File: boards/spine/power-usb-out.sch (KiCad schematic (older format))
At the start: 9 parts

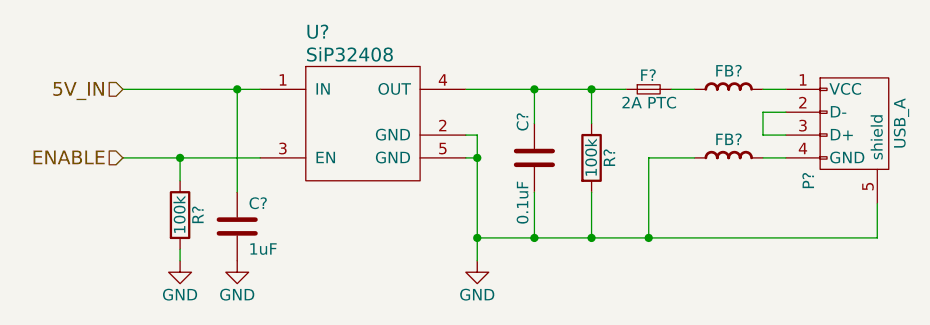
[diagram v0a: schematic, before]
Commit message: Power source switching
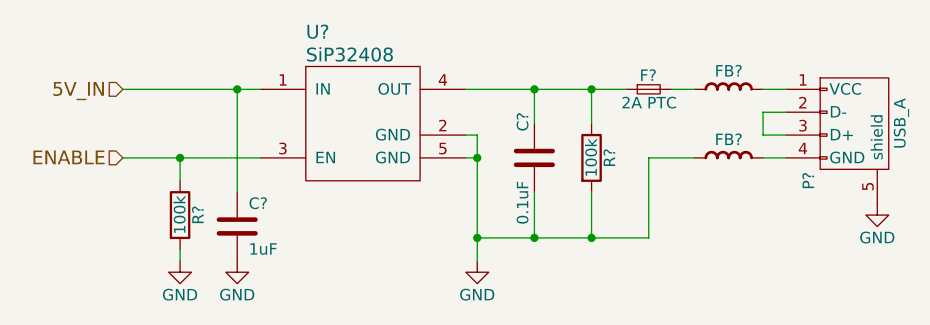
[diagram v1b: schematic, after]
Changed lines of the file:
@@
 	1    0    0    -1
 $EndComp
+$Comp
+L F_Small F?
+U 1 1 564D338C
+P 6400 3700
+F 0 "F?" H 6360 3760 50  0000 L CNN
+F 1 "2A PTC" H 6280 3640 50  0000 L CNN
+F 2 "1812" H 6400 3700 60  0001 C CNN
+F 3 "http://www.belfuse.com/pdfs/0ZCG.pdf" H 6400 3700 60  0001 C CNN
+F 4 "Digikey" H 6400 3700 60  0001 C CNN "Vend1"
+F 5 "507-1777-1-ND" H 6400 3700 60  0001 C CNN "Vend1Id"
+F 6 "Bel Fuse" H 6400 3700 60  0001 C CNN "MfrId"
+F 7 "0ZCG0200FF2C" H 6400 3700 60  0001 C CNN "MfgId"
+F 8 "0.09403" H 6400 3700 60  0001 C CNN "RefPrice1k"
+	1    6400 3700
+	1    0    0    -1
+$EndComp
+Text HLabel 4100 3700 0    60   Input ~ 0
+5V_IN
+Text HLabel 4100 4000 0    60   Input ~ 0
+ENABLE
 Wire Wire Line
 	4350 4450 4350 4400
 Wire Wire Line
-	4100 4000 4350 4000
-Wire Wire Line
-	4350 4000 4700 4000
+	4100 4000 4700 4000
 Wire Wire Line
 	4350 4100 4350 4000
@@
 	5600 4000 5650 4000
 Wire Wire Line
-	5650 3900 5650 4000
-Wire Wire Line
-	5650 4000 5650 4350
-Wire Wire Line
-	5650 4350 5650 4450
+	5650 3900 5650 4450
 Wire Wire Line
 	5600 3900 5650 3900
@@
 Connection ~ 5650 4350
 Wire Wire Line
-	5600 3700 5900 3700
-Wire Wire Line
-	5900 3700 6150 3700
-Wire Wire Line
-	6150 3700 6300 3700
+	5600 3700 6300 3700
 Wire Wire Line
 	5900 3700 5900 3850
@@
 Connection ~ 5900 4350
 Wire Wire Line
-	7400 4350 7400 4200
-Connection ~ 6400 4350
-Wire Wire Line
 	6150 4350 6150 4150
 Connection ~ 6150 4350
@@
 	4600 4150 4600 3700
 Wire Wire Line
-	4100 3700 4600 3700
-Wire Wire Line
-	4600 3700 4700 3700
-$Comp
-L F_Small F?
-U 1 1 564D338C
-P 6400 3700
-F 0 "F?" H 6360 3760 50  0000 L CNN
-F 1 "2A PTC" H 6280 3640 50  0000 L CNN
-F 2 "1812" H 6400 3700 60  0001 C CNN
-F 3 "http://www.belfuse.com/pdfs/0ZCG.pdf" H 6400 3700 60  0001 C CNN
-F 4 "Digikey" H 6400 3700 60  0001 C CNN "Vend1"
-F 5 "507-1777-1-ND" H 6400 3700 60  0001 C CNN "Vend1Id"
-F 6 "Bel Fuse" H 6400 3700 60  0001 C CNN "MfrId"
-F 7 "0ZCG0200FF2C" H 6400 3700 60  0001 C CNN "MfgId"
-F 8 "0.09403" H 6400 3700 60  0001 C CNN "RefPrice1k"
-	1    6400 3700
-	1    0    0    -1
-$EndComp
+	4100 3700 4700 3700
 Wire Wire Line
 	6500 3700 6600 3700
 Wire Wire Line
-	6400 4000 6400 4350
+	6400 4350 6400 4000
+Connection ~ 4600 3700
 Wire Wire Line
-	5650 4350 5900 4350
-Wire Wire Line
-	5900 4350 6150 4350
-Wire Wire Line
-	6150 4350 6400 4350
-Wire Wire Line
-	6400 4350 7400 4350
-Connection ~ 4600 3700
-Text HLabel 4100 3700 0    60   Input ~ 0
-5V_IN
-Text HLabel 4100 4000 0    60   Input ~ 0
-ENABLE
+	5650 4350 6400 4350
+$Comp
+L GND #PWR?
+U 1 1 564CFCD3
+P 7400 4200
+F 0 "#PWR?" H 7400 3950 50  0001 C CNN
+F 1 "GND" H 7400 4050 50  0000 C CNN
+F 2 "" H 7400 4200 60  0000 C CNN
+F 3 "" H 7400 4200 60  0000 C CNN
+	1    7400 4200
+	1    0    0    -1
+$EndComp
 $EndSCHEMATC

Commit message: Power management and such
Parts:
- added C64: 0.1uF, 0805, symbol C
- P3: renamed from P?; value USB_A -> USB-A; MfgId (none) -> USB-A1SSW6; MfrId (none) -> On-Shore Tech; RefPrice1k (none) -> 0.35310; Vend1 (none) -> Digikey; Vend1Id (none) -> ED2991-ND
- U10: renamed from U?; MfgId (none) -> Vishay; MfrId (none) -> SIP32408DNP-T1-GE4; RefPrice1k (none) -> 0.175; Vend1 (none) -> Digikey; Vend1Id (none) -> SIP32408DNP-T1-GE4CT-ND
- gave numbers to parts that had none: 7
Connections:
- net GND: now also C64.1
- net at F1.2, FB5.1: now also C64.2
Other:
- note added: "Not the main +5V rail; this is intended to draw power\nfrom the DC-DC converter only, not the USB-B input."
- moved on the sheet: C62, C63, F1, FB5, FB6, P3, R29, R30, U10

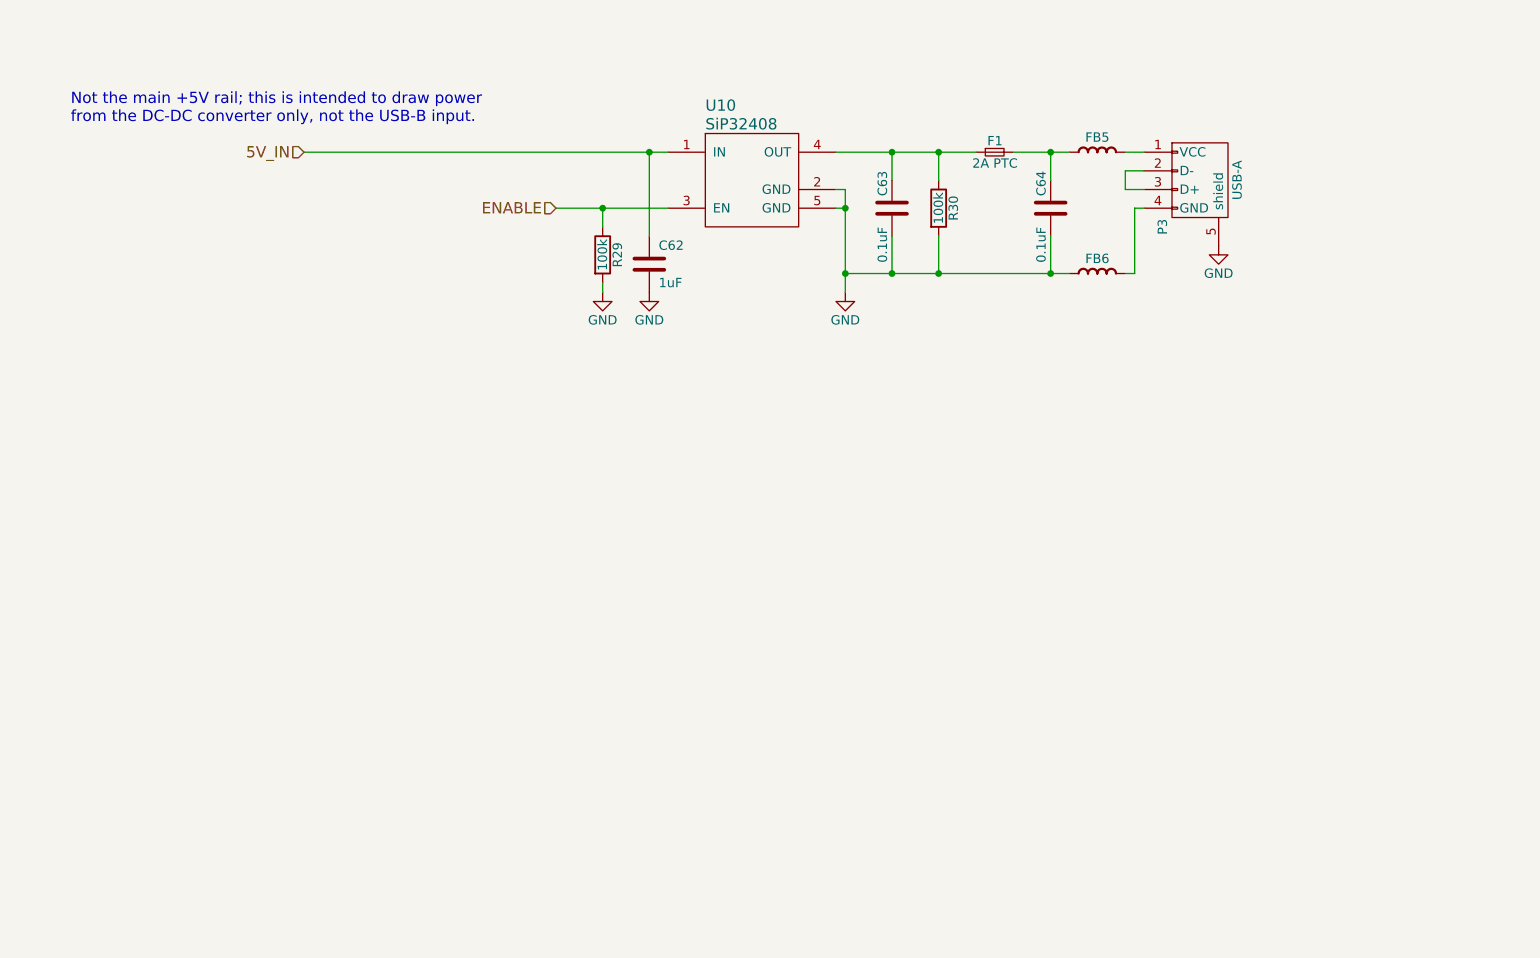
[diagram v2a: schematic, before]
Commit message: Clock generator, sync connectors, title blocks
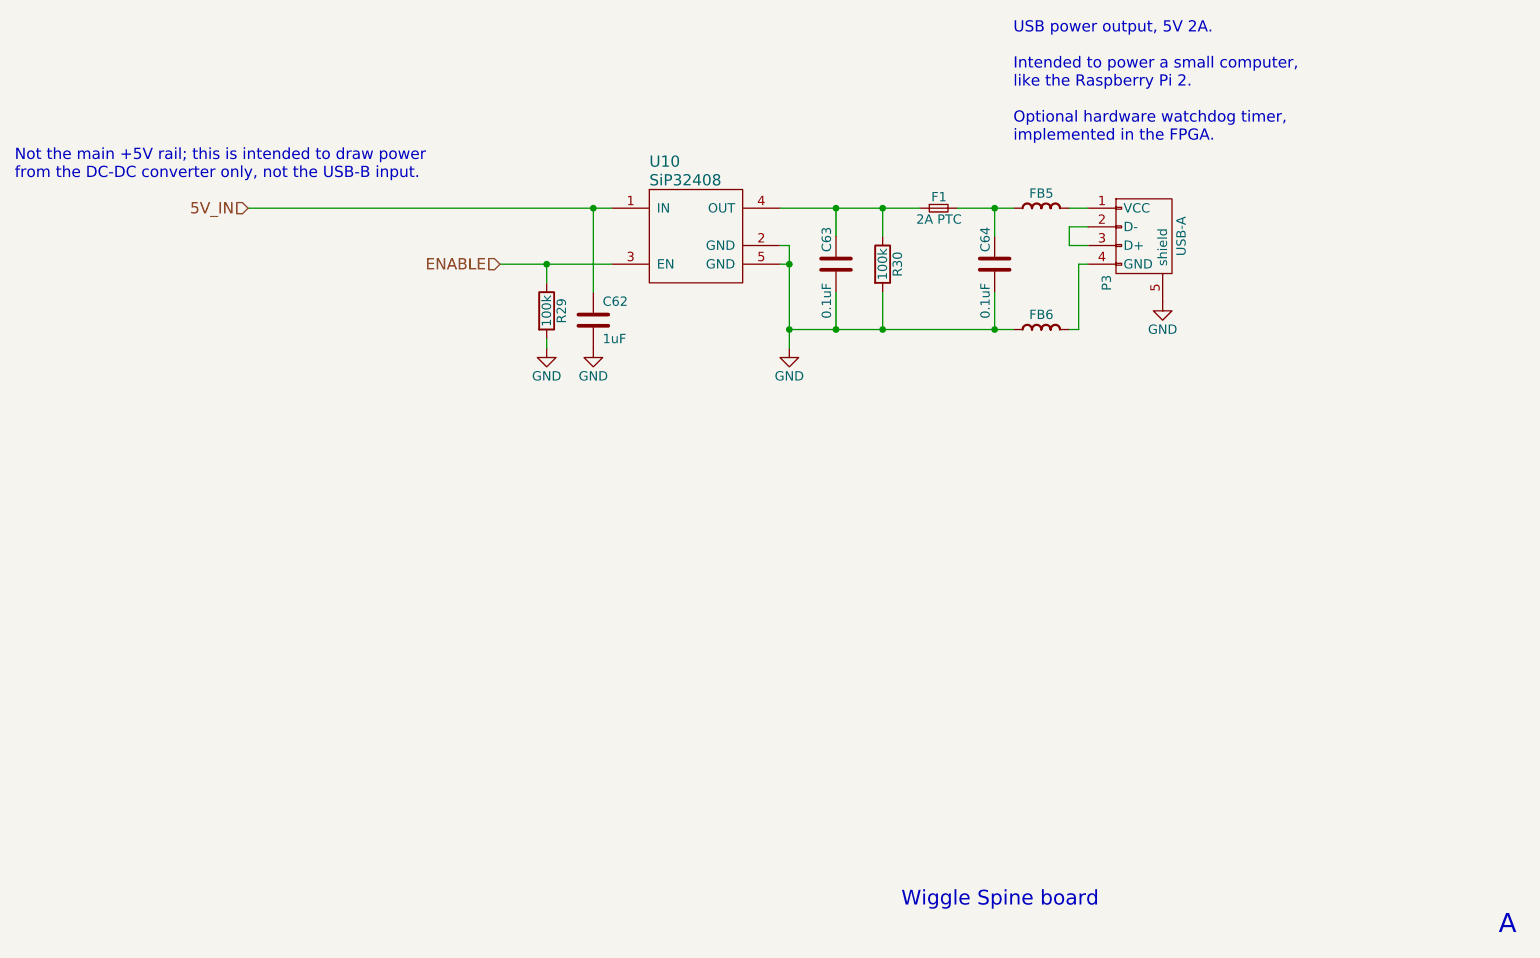
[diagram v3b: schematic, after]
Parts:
- C62, C63, C64: footprint 0805 -> Capacitors_SMD:C_0805
- R29, R30: footprint (none) -> Resistors_SMD:R_0805
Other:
- note added: "A"
- note added: "USB power output, 5V 2A.\n\nIntended to power a small computer,\nlike the Raspberry Pi 2.\n\nOptional hardware watchdog timer,\nimplemented in the FPGA."
- note added: "Wiggle Spine board"
- moved on the sheet: C62, C63, C64, F1, FB5, FB6, P3, R29, R30, U10

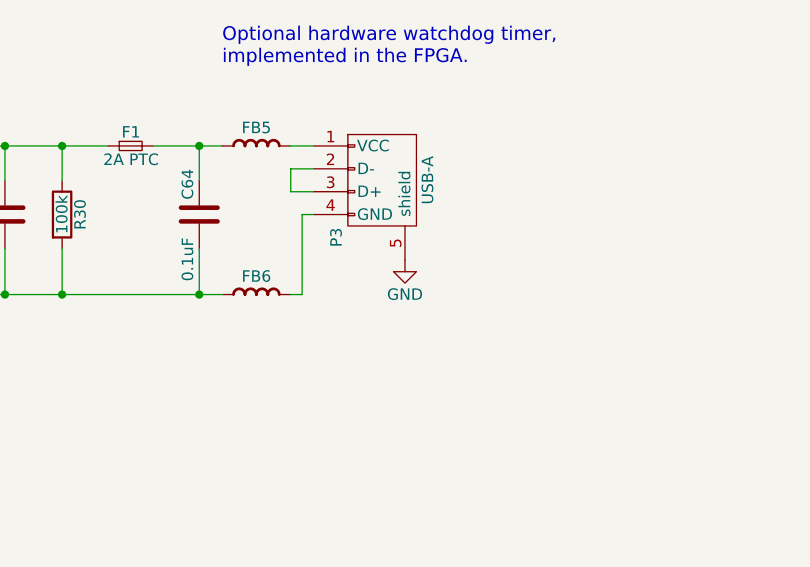
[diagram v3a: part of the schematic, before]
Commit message: Fixes for shield grounds and module numbering
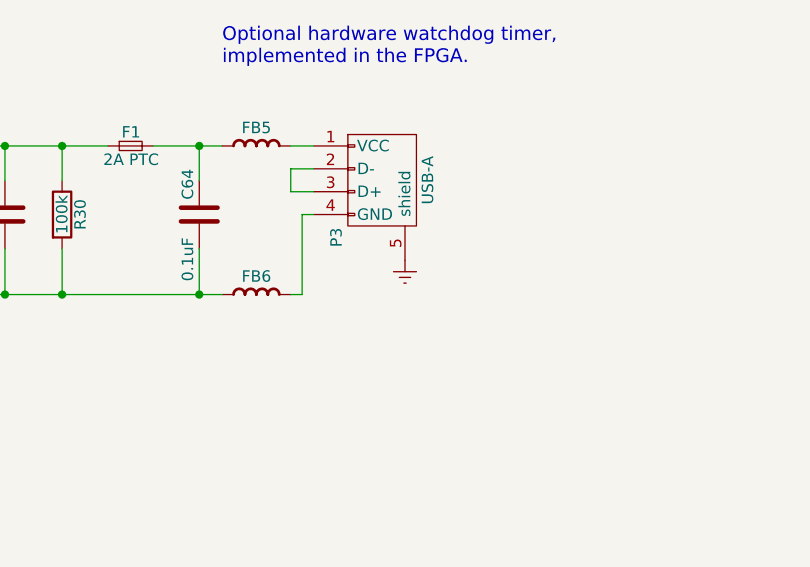
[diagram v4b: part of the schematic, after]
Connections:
- net GND: no longer P3.5 (shield)
- new net Earth: P3.5 (shield)
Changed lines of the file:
@@
 $EndComp
 $Comp
-L GND #PWR0130
+L GND #PWR0131
 U 1 1 564D3372
 P 4800 4750
-F 0 "#PWR0130" H 4800 4500 50  0001 C CNN
+F 0 "#PWR0131" H 4800 4500 50  0001 C CNN
 F 1 "GND" H 4800 4600 50  0000 C CNN
 F 2 "" H 4800 4750 60  0000 C CNN
@@
 $EndComp
 $Comp
-L GND #PWR0131
+L GND #PWR0132
 U 1 1 564D3375
 P 6100 4750
-F 0 "#PWR0131" H 6100 4500 50  0001 C CNN
+F 0 "#PWR0132" H 6100 4500 50  0001 C CNN
 F 1 "GND" H 6100 4600 50  0000 C CNN
 F 2 "" H 6100 4750 60  0000 C CNN
@@
 $EndComp
 $Comp
-L GND #PWR0132
+L GND #PWR0133
 U 1 1 564D337A
 P 5050 4750
-F 0 "#PWR0132" H 5050 4500 50  0001 C CNN
+F 0 "#PWR0133" H 5050 4500 50  0001 C CNN
 F 1 "GND" H 5050 4600 50  0000 C CNN
 F 2 "" H 5050 4750 60  0000 C CNN
@@
 	7000 4000 7300 4000
 Connection ~ 5050 4000
-$Comp
-L GND #PWR0133
-U 1 1 564CFCD3
-P 8100 4500
-F 0 "#PWR0133" H 8100 4250 50  0001 C CNN
-F 1 "GND" H 8100 4350 50  0000 C CNN
-F 2 "" H 8100 4500 60  0000 C CNN
-F 3 "" H 8100 4500 60  0000 C CNN
-	1    8100 4500
-	1    0    0    -1
-$EndComp
 Wire Wire Line
 	7600 4650 7650 4650
@@
 Text Notes 9900 7900 0    102  ~ 0
 A
+$Comp
+L Earth #PWR0134
+U 1 1 565B70B7
+P 8100 4500
+F 0 "#PWR0134" H 8100 4250 50  0001 C CNN
+F 1 "Earth" H 8100 4350 50  0001 C CNN
+F 2 "" H 8100 4500 60  0000 C CNN
+F 3 "" H 8100 4500 60  0000 C CNN
+	1    8100 4500
+	1    0    0    -1
+$EndComp
 $EndSCHEMATC

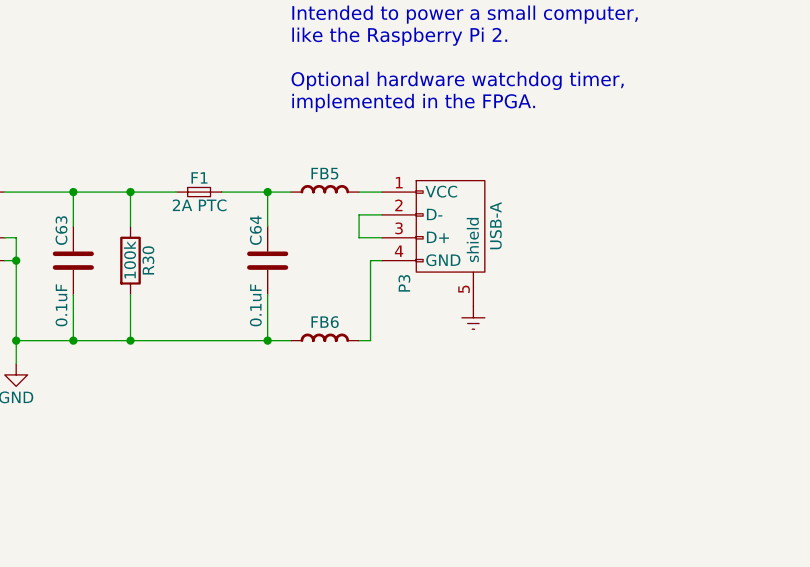
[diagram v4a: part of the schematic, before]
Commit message: Schematic footprint and refdes work
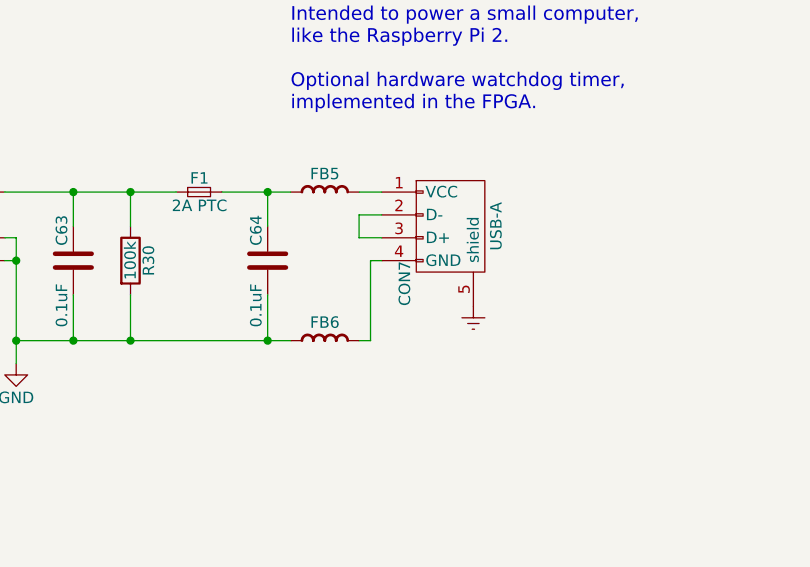
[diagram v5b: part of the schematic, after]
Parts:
- CON7: renamed from P3; footprint (none) -> Connect:USB_A_Vertical
- F1: footprint 1812 -> Resistors_SMD:R_1812
- FB5, FB6: footprint (none) -> Resistors_SMD:R_0805
- U10: footprint (none) -> TDFN4:TDFN4
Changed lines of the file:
@@
 F 0 "U10" H 5350 4350 60  0000 L CNN
 F 1 "SiP32408" H 5350 4250 60  0000 L CNN
-F 2 "" H 5650 4250 60  0001 C CNN
+F 2 "TDFN4:TDFN4" H 5650 4250 60  0001 C CNN
 F 3 "http://www.vishay.com/docs/63717/sip32408.pdf" H 5650 4250 60  0001 C CNN
 F 4 "Digikey" H 5600 4050 60  0001 C CNN "Vend1"
@@
 $EndComp
 $Comp
-L GND #PWR0131
+L GND #PWR131
 U 1 1 564D3372
 P 4800 4750
-F 0 "#PWR0131" H 4800 4500 50  0001 C CNN
+F 0 "#PWR131" H 4800 4500 50  0001 C CNN
 F 1 "GND" H 4800 4600 50  0000 C CNN
 F 2 "" H 4800 4750 60  0000 C CNN
@@
 $EndComp
 $Comp
-L USB_A P3
+L USB_A CON7
 U 1 1 564D3373
 P 8000 4200
-F 0 "P3" H 8200 4000 50  0000 C CNN
+F 0 "CON7" H 8200 4000 50  0000 C CNN
 F 1 "USB-A" H 7950 4400 50  0000 C CNN
-F 2 "" V 7950 4100 60  0001 C CNN
+F 2 "Connect:USB_A_Vertical" V 7950 4100 60  0001 C CNN
 F 3 "http://www.on-shore.com/sites/default/files/manuals/usb-a1ssxx.pdf" V 7950 4100 60  0001 C CNN
 F 4 "0.35310" H 8000 4200 60  0001 C CNN "RefPrice1k"
@@
 F 0 "FB5" H 7450 4050 50  0000 C BNN
 F 1 "Ferrite bead" H 7700 4050 39  0001 C BNN
-F 2 "" H 7300 4150 50  0001 C CNN
+F 2 "Resistors_SMD:R_0805" H 7300 4150 50  0001 C CNN
 F 3 "http://www.samsungsem.com/kr/front/downloadcms.do?path=/kr/support/product-search/bead/__icsFiles/afieldfile/2014/11/13&fileName=S_CIB21P110NE.pdf" H 7325 4000 60  0001 C CNN
 F 4 "0.00906" H 7300 4000 60  0001 C CNN "RefPrice1k"
@@
 $EndComp
 $Comp
-L GND #PWR0132
+L GND #PWR133
 U 1 1 564D3375
 P 6100 4750
-F 0 "#PWR0132" H 6100 4500 50  0001 C CNN
+F 0 "#PWR133" H 6100 4500 50  0001 C CNN
 F 1 "GND" H 6100 4600 50  0000 C CNN
 F 2 "" H 6100 4750 60  0000 C CNN
@@
 F 0 "FB6" H 7450 4700 50  0000 C BNN
 F 1 "Ferrite bead" H 7700 4700 39  0001 C BNN
-F 2 "" H 7300 4800 50  0001 C CNN
+F 2 "Resistors_SMD:R_0805" H 7300 4800 50  0001 C CNN
 F 3 "http://www.samsungsem.com/kr/front/downloadcms.do?path=/kr/support/product-search/bead/__icsFiles/afieldfile/2014/11/13&fileName=S_CIB21P110NE.pdf" H 7325 4650 60  0001 C CNN
 F 4 "0.00906" H 7300 4650 60  0001 C CNN "RefPrice1k"
@@
 $EndComp
 $Comp
-L GND #PWR0133
+L GND #PWR132
 U 1 1 564D337A
 P 5050 4750
-F 0 "#PWR0133" H 5050 4500 50  0001 C CNN
+F 0 "#PWR132" H 5050 4500 50  0001 C CNN
 F 1 "GND" H 5050 4600 50  0000 C CNN
 F 2 "" H 5050 4750 60  0000 C CNN
@@
 F 0 "F1" H 6860 4060 50  0000 L CNN
 F 1 "2A PTC" H 6780 3940 50  0000 L CNN
-F 2 "1812" H 6900 4000 60  0001 C CNN
+F 2 "Resistors_SMD:R_1812" H 6900 4000 60  0001 C CNN
 F 3 "http://www.belfuse.com/pdfs/0ZCG.pdf" H 6900 4000 60  0001 C CNN
 F 4 "Digikey" H 6900 4000 60  0001 C CNN "Vend1"
@@
 A
 $Comp
-L Earth #PWR0134
+L Earth #PWR134
 U 1 1 565B70B7
 P 8100 4500
-F 0 "#PWR0134" H 8100 4250 50  0001 C CNN
+F 0 "#PWR134" H 8100 4250 50  0001 C CNN
 F 1 "Earth" H 8100 4350 50  0001 C CNN
 F 2 "" H 8100 4500 60  0000 C CNN
